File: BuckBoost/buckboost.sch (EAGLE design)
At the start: 8 parts

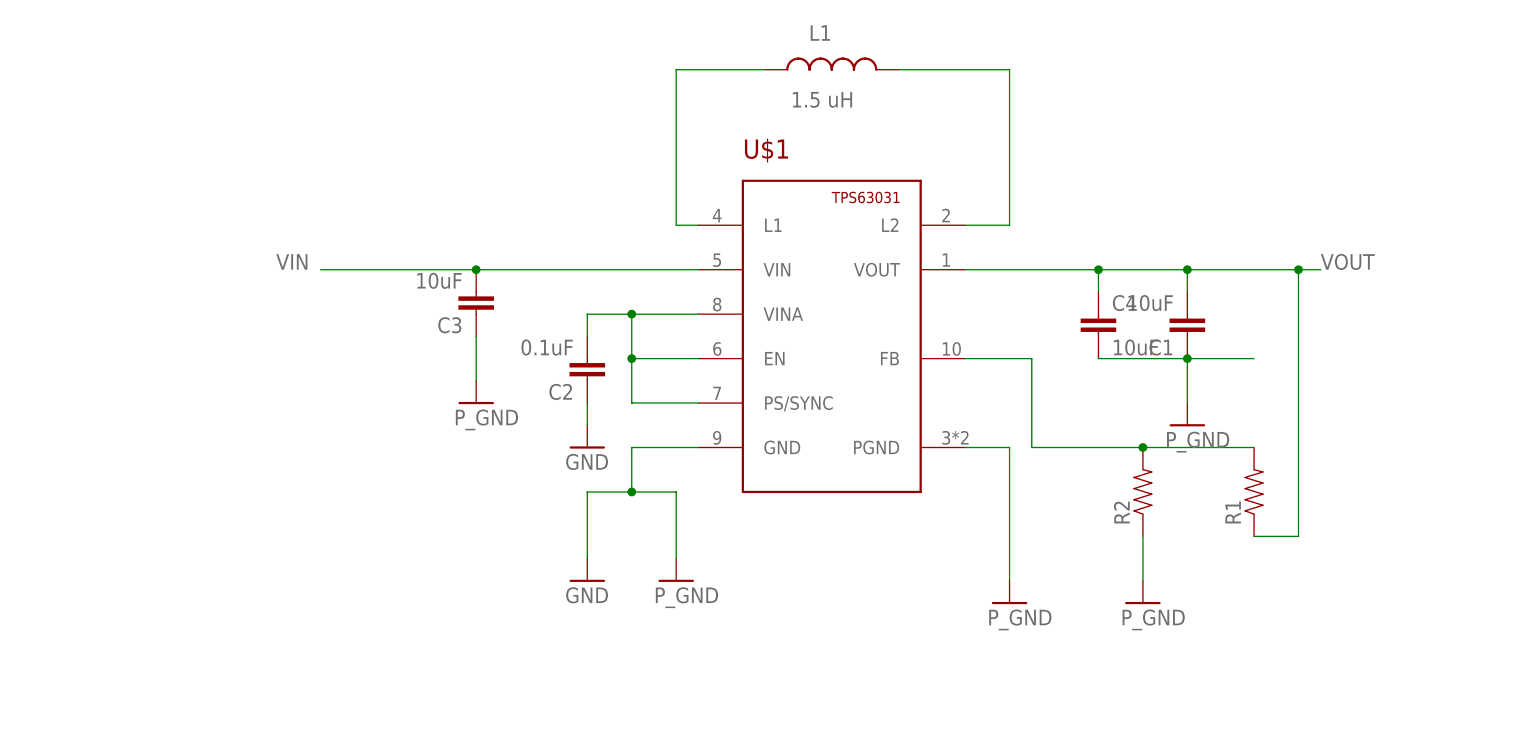
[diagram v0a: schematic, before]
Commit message: Changed Resistor and Capacity sizes
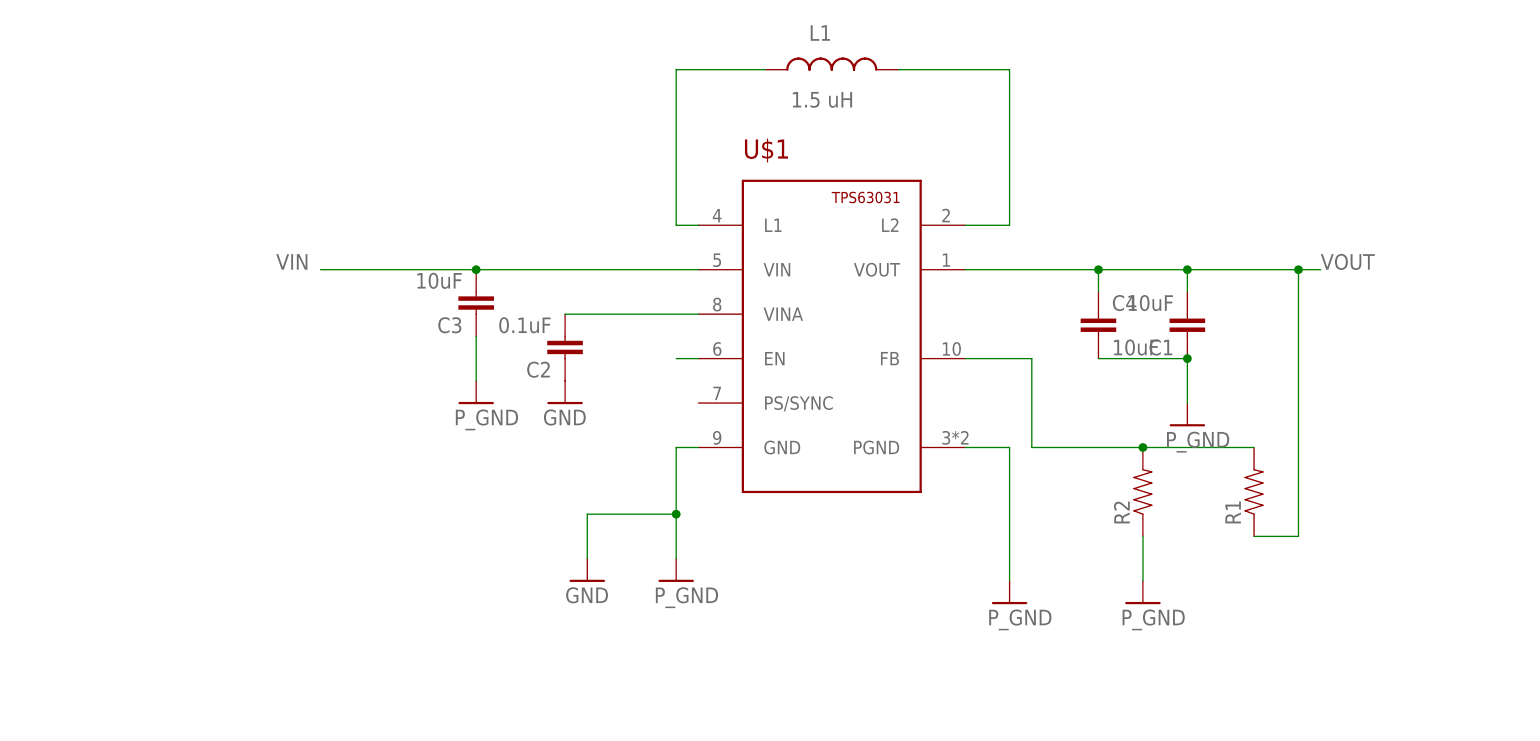
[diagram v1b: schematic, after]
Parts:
- C1, C2, C3, C4: device SparkFun-Passives:CAP0603-CAP -> SparkFun-Capacitors:CAP1206
- R1, R2: device SparkFun-Resistors:RESISTOR0603 -> SparkFun-Resistors:RESISTOR1206
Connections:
- new net N$2: U$1.EN
- net N$3: no longer U$1.EN, U$1.PS/SYNC
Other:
- moved on the sheet: C2
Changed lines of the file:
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@@
 <part name="U$1" library="Capstone Library" deviceset="TPS63031" device=""/>
 <part name="L1" library="Capstone Library" deviceset="INDUCTOR" device="" value="1.5 uH"/>
-<part name="C1" library="SparkFun-Passives" deviceset="CAP" device="0603-CAP" value="10uF"/>
-<part name="C2" library="SparkFun-Passives" deviceset="CAP" device="0603-CAP" value="0.1uF"/>
-<part name="C3" library="SparkFun-Passives" deviceset="CAP" device="0603-CAP" value="10uF"/>
-<part name="C4" library="SparkFun-Passives" deviceset="CAP" device="0603-CAP" value="10uF"/>
-<part name="R1" library="SparkFun-Resistors" deviceset="RESISTOR" device="0603"/>
-<part name="R2" library="SparkFun-Resistors" deviceset="RESISTOR" device="0603"/>
+<part name="C1" library="SparkFun-Capacitors" deviceset="CAP" device="1206" value="10uF"/>
+<part name="C2" library="SparkFun-Capacitors" deviceset="CAP" device="1206" value="0.1uF"/>
+<part name="C3" library="SparkFun-Capacitors" deviceset="CAP" device="1206" value="10uF"/>
+<part name="C4" library="SparkFun-Capacitors" deviceset="CAP" device="1206" value="10uF"/>
+<part name="R1" library="SparkFun-Resistors" deviceset="RESISTOR" device="1206"/>
+<part name="R2" library="SparkFun-Resistors" deviceset="RESISTOR" device="1206"/>
 <part name="GND1" library="SparkFun-Aesthetics" deviceset="GND" device=""/>
 <part name="GND2" library="SparkFun-Aesthetics" deviceset="GND" device="" value="P_GND"/>
@@
 </instance>
 <instance part="C1" gate="G$1" x="205.74" y="-22.86" rot="R180"/>
-<instance part="C2" gate="G$1" x="137.16" y="-27.94" rot="R180"/>
+<instance part="C2" gate="G$1" x="134.62" y="-25.4" rot="R180"/>
 <instance part="C3" gate="G$1" x="124.46" y="-20.32" rot="R180"/>
 <instance part="C4" gate="G$1" x="195.58" y="-25.4"/>
@@
 <instance part="GND4" gate="1" x="205.74" y="-35.56"/>
 <instance part="P_GND" gate="1" x="124.46" y="-33.02"/>
-<instance part="GND6" gate="1" x="137.16" y="-38.1"/>
+<instance part="GND6" gate="1" x="134.62" y="-33.02"/>
 <instance part="P_GND1" gate="1" x="200.66" y="-55.88"/>
 </instances>
@@
 <segment>
 <pinref part="U$1" gate="G$1" pin="VINA"/>
-<wire x1="149.86" y1="-22.86" x2="142.24" y2="-22.86" width="0.1524" layer="91"/>
 <pinref part="C2" gate="G$1" pin="2"/>
-<wire x1="142.24" y1="-22.86" x2="137.16" y2="-22.86" width="0.1524" layer="91"/>
-<wire x1="137.16" y1="-22.86" x2="137.16" y2="-25.4" width="0.1524" layer="91"/>
-<pinref part="U$1" gate="G$1" pin="PS/SYNC"/>
-<wire x1="149.86" y1="-33.02" x2="142.24" y2="-33.02" width="0.1524" layer="91"/>
-<wire x1="142.24" y1="-33.02" x2="142.24" y2="-27.94" width="0.1524" layer="91"/>
-<junction x="142.24" y="-22.86"/>
-<pinref part="U$1" gate="G$1" pin="EN"/>
-<wire x1="142.24" y1="-27.94" x2="142.24" y2="-22.86" width="0.1524" layer="91"/>
-<wire x1="149.86" y1="-27.94" x2="142.24" y2="-27.94" width="0.1524" layer="91"/>
-<junction x="142.24" y="-27.94"/>
+<wire x1="149.86" y1="-22.86" x2="134.62" y2="-22.86" width="0.1524" layer="91"/>
 </segment>
 </net>
@@
 <pinref part="C1" gate="G$1" pin="1"/>
 <wire x1="205.74" y1="-27.94" x2="205.74" y2="-33.02" width="0.1524" layer="91"/>
-<wire x1="205.74" y1="-27.94" x2="213.36" y2="-27.94" width="0.1524" layer="91"/>
 <junction x="205.74" y="-27.94"/>
 <pinref part="C4" gate="G$1" pin="2"/>
@@
 <pinref part="C2" gate="G$1" pin="1"/>
 <pinref part="GND6" gate="1" pin="GND"/>
-<wire x1="137.16" y1="-33.02" x2="137.16" y2="-35.56" width="0.1524" layer="91"/>
-</segment>
-<segment>
-<pinref part="U$1" gate="G$1" pin="GND"/>
-<wire x1="149.86" y1="-38.1" x2="142.24" y2="-38.1" width="0.1524" layer="91"/>
-<wire x1="142.24" y1="-38.1" x2="142.24" y2="-43.18" width="0.1524" layer="91"/>
-<wire x1="142.24" y1="-43.18" x2="147.32" y2="-43.18" width="0.1524" layer="91"/>
-<wire x1="142.24" y1="-43.18" x2="137.16" y2="-43.18" width="0.1524" layer="91"/>
-<junction x="142.24" y="-43.18"/>
-<pinref part="GND1" gate="1" pin="GND"/>
-<wire x1="137.16" y1="-50.8" x2="137.16" y2="-43.18" width="0.1524" layer="91"/>
-<pinref part="GND2" gate="1" pin="GND"/>
-<wire x1="147.32" y1="-50.8" x2="147.32" y2="-43.18" width="0.1524" layer="91"/>
 </segment>
 <segment>
@@
 <wire x1="185.42" y1="-38.1" x2="185.42" y2="-53.34" width="0.1524" layer="91"/>
 </segment>
+<segment>
+<pinref part="U$1" gate="G$1" pin="GND"/>
+<pinref part="GND2" gate="1" pin="GND"/>
+<wire x1="149.86" y1="-38.1" x2="147.32" y2="-38.1" width="0.1524" layer="91"/>
+<wire x1="147.32" y1="-38.1" x2="147.32" y2="-45.72" width="0.1524" layer="91"/>
+<pinref part="GND1" gate="1" pin="GND"/>
+<wire x1="147.32" y1="-45.72" x2="147.32" y2="-50.8" width="0.1524" layer="91"/>
+<wire x1="147.32" y1="-45.72" x2="137.16" y2="-45.72" width="0.1524" layer="91"/>
+<wire x1="137.16" y1="-45.72" x2="137.16" y2="-50.8" width="0.1524" layer="91"/>
+<junction x="147.32" y="-45.72"/>
+</segment>
 </net>
+<net name="N$2" class="0">
+<segment>
+<pinref part="U$1" gate="G$1" pin="EN"/>
+<wire x1="147.32" y1="-27.94" x2="149.86" y2="-27.94" width="0.1524" layer="91"/>
+</segment>
+</net>

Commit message: PCB finished, only need to fix labels
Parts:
- added J1: (no value), SparkFun-Connectors:M04PTH
- added J2: (no value), SparkFun-Connectors:M05PTH
- added SJ1, SJ2: SOLDERJUMPERNC, SparkFun-Retired:SOLDERJUMPERNC
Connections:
- new net N$4: SJ2.2, U$1.PS/SYNC
- net GND: now also J2.2, J2.3, SJ2.1
- net N$2: now also SJ1.2
- net VIN: now also J2.1, J2.4, J2.5, SJ1.1
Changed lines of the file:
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@@
 <layer number="112" name="tSilk" color="7" fill="1" visible="yes" active="yes"/>
 <layer number="113" name="IDFDebug" color="4" fill="1" visible="yes" active="yes"/>
+<layer number="114" name="Badge_Outline" color="7" fill="1" visible="yes" active="yes"/>
+<layer number="115" name="ReferenceISLANDS" color="7" fill="1" visible="yes" active="yes"/>
 <layer number="116" name="Patch_BOT" color="9" fill="4" visible="no" active="yes"/>
 <layer number="118" name="Rect_Pads" color="7" fill="1" visible="no" active="no"/>
@@
 <part name="GND6" library="SparkFun-Aesthetics" deviceset="GND" device=""/>
 <part name="P_GND1" library="SparkFun-Aesthetics" deviceset="GND" device="" value="P_GND"/>
+<part name="J1" library="SparkFun-Connectors" deviceset="M04" device="PTH"/>
+<part name="J2" library="SparkFun-Connectors" deviceset="M05" device="PTH"/>
+<part name="SJ1" library="SparkFun-Retired" deviceset="SOLDERJUMPER" device="NC"/>
+<part name="P_GND2" library="SparkFun-Aesthetics" deviceset="GND" device="" value="P_GND"/>
+<part name="SJ2" library="SparkFun-Retired" deviceset="SOLDERJUMPER" device="NC"/>
+<part name="GND5" library="SparkFun-Aesthetics" deviceset="GND" device=""/>
 </parts>
 <sheets>
@@
 <instance part="GND6" gate="1" x="134.62" y="-33.02"/>
 <instance part="P_GND1" gate="1" x="200.66" y="-55.88"/>
+<instance part="J1" gate="G$1" x="238.76" y="-20.32" rot="R180"/>
+<instance part="J2" gate="G$1" x="83.82" y="-22.86"/>
+<instance part="SJ1" gate="1" x="109.22" y="-45.72" smashed="yes" rot="R90">
+<attribute name="NAME" x="106.68" y="-48.26" size="1.778" layer="95" rot="R90"/>
+<attribute name="VALUE" x="116.84" y="-53.34" size="1.778" layer="96" rot="R180"/>
+</instance>
+<instance part="P_GND2" gate="1" x="101.6" y="-27.94"/>
+<instance part="SJ2" gate="1" x="124.46" y="-55.88" rot="R90"/>
+<instance part="GND5" gate="1" x="124.46" y="-66.04"/>
 </instances>
 <busses>
@@
 <wire x1="149.86" y1="-17.78" x2="124.46" y2="-17.78" width="0.1524" layer="91"/>
 <junction x="124.46" y="-17.78"/>
-<wire x1="124.46" y1="-17.78" x2="106.68" y2="-17.78" width="0.1524" layer="91"/>
-<label x="101.6" y="-17.78" size="1.778" layer="95"/>
+<wire x1="124.46" y1="-17.78" x2="93.98" y2="-17.78" width="0.1524" layer="91"/>
+<label x="96.52" y="-12.7" size="1.778" layer="95"/>
+<pinref part="J2" gate="G$1" pin="5"/>
+<pinref part="J2" gate="G$1" pin="4"/>
+<wire x1="93.98" y1="-17.78" x2="91.44" y2="-17.78" width="0.1524" layer="91"/>
+<wire x1="91.44" y1="-17.78" x2="91.44" y2="-20.32" width="0.1524" layer="91"/>
+<wire x1="93.98" y1="-17.78" x2="93.98" y2="-7.62" width="0.1524" layer="91"/>
+<junction x="93.98" y="-17.78"/>
+<wire x1="93.98" y1="-7.62" x2="73.66" y2="-7.62" width="0.1524" layer="91"/>
+<wire x1="73.66" y1="-7.62" x2="73.66" y2="-45.72" width="0.1524" layer="91"/>
+<pinref part="J2" gate="G$1" pin="1"/>
+<wire x1="91.44" y1="-27.94" x2="96.52" y2="-27.94" width="0.1524" layer="91"/>
+<wire x1="96.52" y1="-27.94" x2="96.52" y2="-45.72" width="0.1524" layer="91"/>
+<pinref part="SJ1" gate="1" pin="1"/>
+<wire x1="96.52" y1="-45.72" x2="96.52" y2="-50.8" width="0.1524" layer="91"/>
+<wire x1="96.52" y1="-50.8" x2="109.22" y2="-50.8" width="0.1524" layer="91"/>
+<wire x1="73.66" y1="-45.72" x2="96.52" y2="-45.72" width="0.1524" layer="91"/>
+<junction x="96.52" y="-45.72"/>
 </segment>
 </net>
@@
 <junction x="147.32" y="-45.72"/>
 </segment>
+<segment>
+<pinref part="J2" gate="G$1" pin="3"/>
+<wire x1="91.44" y1="-22.86" x2="101.6" y2="-22.86" width="0.1524" layer="91"/>
+<pinref part="P_GND2" gate="1" pin="GND"/>
+<wire x1="101.6" y1="-22.86" x2="101.6" y2="-25.4" width="0.1524" layer="91"/>
+<pinref part="J2" gate="G$1" pin="2"/>
+<wire x1="91.44" y1="-25.4" x2="101.6" y2="-25.4" width="0.1524" layer="91"/>
+<junction x="101.6" y="-25.4"/>
+</segment>
+<segment>
+<pinref part="SJ2" gate="1" pin="1"/>
+<pinref part="GND5" gate="1" pin="GND"/>
+<wire x1="124.46" y1="-60.96" x2="124.46" y2="-63.5" width="0.1524" layer="91"/>
+</segment>
 </net>
 <net name="N$2" class="0">
 <segment>
 <pinref part="U$1" gate="G$1" pin="EN"/>
-<wire x1="147.32" y1="-27.94" x2="149.86" y2="-27.94" width="0.1524" layer="91"/>
-</segment>
-</net>
+<wire x1="149.86" y1="-27.94" x2="142.24" y2="-27.94" width="0.1524" layer="91"/>
+<pinref part="SJ1" gate="1" pin="2"/>
+<wire x1="109.22" y1="-40.64" x2="142.24" y2="-40.64" width="0.1524" layer="91"/>
+<wire x1="142.24" y1="-40.64" x2="142.24" y2="-27.94" width="0.1524" layer="91"/>
+</segment>
+</net>
+<net name="N$4" class="0">
+<segment>
+<pinref part="U$1" gate="G$1" pin="PS/SYNC"/>
+<wire x1="149.86" y1="-33.02" x2="144.78" y2="-33.02" width="0.1524" layer="91"/>
+<wire x1="144.78" y1="-33.02" x2="144.78" y2="-43.18" width="0.1524" layer="91"/>
+<pinref part="SJ2" gate="1" pin="2"/>
+<wire x1="144.78" y1="-43.18" x2="124.46" y2="-43.18" width="0.1524" layer="91"/>
+<wire x1="124.46" y1="-43.18" x2="124.46" y2="-50.8" width="0.1524" layer="91"/>
+</segment>
+</net>

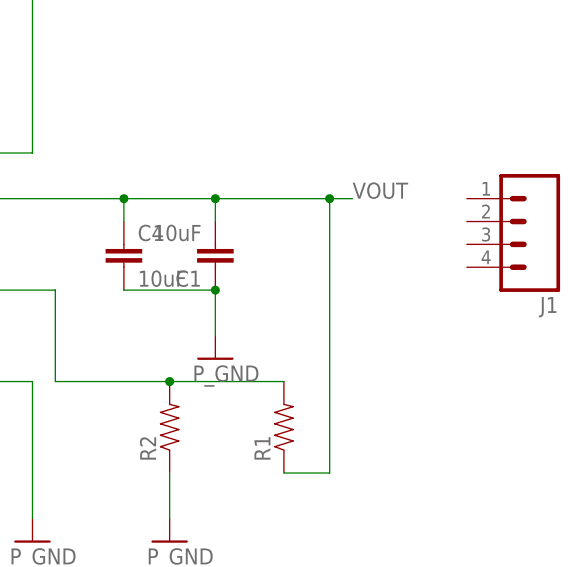
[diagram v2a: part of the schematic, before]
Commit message: Finshed VOUT, just labels
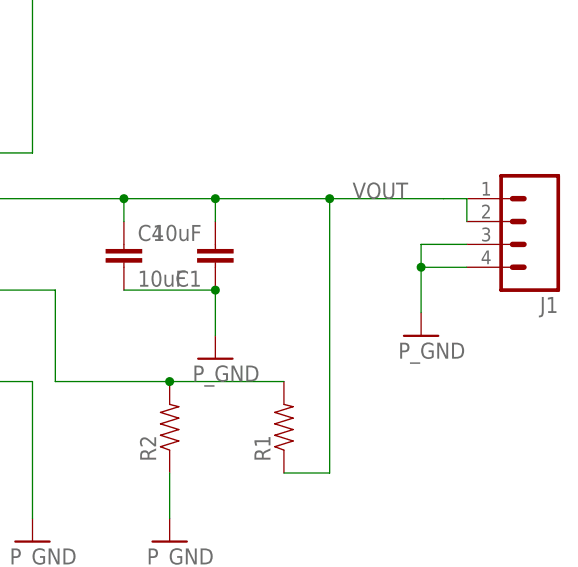
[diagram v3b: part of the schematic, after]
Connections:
- net GND: now also J1.3, J1.4
- net VOUT: now also J1.1, J1.2
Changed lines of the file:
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@@
 <part name="SJ2" library="SparkFun-Retired" deviceset="SOLDERJUMPER" device="NC"/>
 <part name="GND5" library="SparkFun-Aesthetics" deviceset="GND" device=""/>
+<part name="P_GND3" library="SparkFun-Aesthetics" deviceset="GND" device="" value="P_GND"/>
 </parts>
 <sheets>
@@
 <instance part="SJ2" gate="1" x="124.46" y="-55.88" rot="R90"/>
 <instance part="GND5" gate="1" x="124.46" y="-66.04"/>
+<instance part="P_GND3" gate="1" x="228.6" y="-33.02"/>
 </instances>
 <busses>
@@
 <pinref part="R1" gate="G$1" pin="1"/>
 <wire x1="218.44" y1="-48.26" x2="213.36" y2="-48.26" width="0.1524" layer="91"/>
-<wire x1="218.44" y1="-17.78" x2="220.98" y2="-17.78" width="0.1524" layer="91"/>
 <junction x="218.44" y="-17.78"/>
+<pinref part="J1" gate="G$1" pin="1"/>
+<wire x1="218.44" y1="-17.78" x2="231.14" y2="-17.78" width="0.1524" layer="91"/>
+<pinref part="J1" gate="G$1" pin="2"/>
+<wire x1="231.14" y1="-17.78" x2="233.68" y2="-17.78" width="0.1524" layer="91"/>
+<wire x1="233.68" y1="-17.78" x2="233.68" y2="-20.32" width="0.1524" layer="91"/>
 </segment>
 </net>
@@
 <wire x1="124.46" y1="-60.96" x2="124.46" y2="-63.5" width="0.1524" layer="91"/>
 </segment>
+<segment>
+<pinref part="J1" gate="G$1" pin="3"/>
+<pinref part="P_GND3" gate="1" pin="GND"/>
+<wire x1="233.68" y1="-22.86" x2="228.6" y2="-22.86" width="0.1524" layer="91"/>
+<wire x1="228.6" y1="-22.86" x2="228.6" y2="-25.4" width="0.1524" layer="91"/>
+<pinref part="J1" gate="G$1" pin="4"/>
+<wire x1="228.6" y1="-25.4" x2="228.6" y2="-30.48" width="0.1524" layer="91"/>
+<wire x1="233.68" y1="-25.4" x2="228.6" y2="-25.4" width="0.1524" layer="91"/>
+<junction x="228.6" y="-25.4"/>
+</segment>
 </net>

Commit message: added 6 header
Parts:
- added J3: (no value), SparkFun-Connectors:M06SILK_FEMALE_PTH
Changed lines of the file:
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@@
 <part name="GND5" library="SparkFun-Aesthetics" deviceset="GND" device=""/>
 <part name="P_GND3" library="SparkFun-Aesthetics" deviceset="GND" device="" value="P_GND"/>
+<part name="J3" library="SparkFun-Connectors" deviceset="M06" device="SILK_FEMALE_PTH"/>
 </parts>
 <sheets>
@@
 <instance part="GND5" gate="1" x="124.46" y="-66.04"/>
 <instance part="P_GND3" gate="1" x="228.6" y="-33.02"/>
+<instance part="J3" gate="G$1" x="78.74" y="-60.96"/>
 </instances>
 <busses>
